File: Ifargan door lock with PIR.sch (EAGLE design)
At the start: 41 parts, among them K1 Relay, K2 Relay, Q1 2N2905, Q2 2N2219, T1 PAD_TERMINAL-4.1MMROUND, T10 PAD_TERMINAL-4.1MMROUND, T11 PAD_TERMINAL-4.1MMROUND, T12 PAD_TERMINAL-4.1MMROUND, T13 PAD_TERMINAL-4.1MMROUND, T14 PAD_TERMINAL-4.1MMROUND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

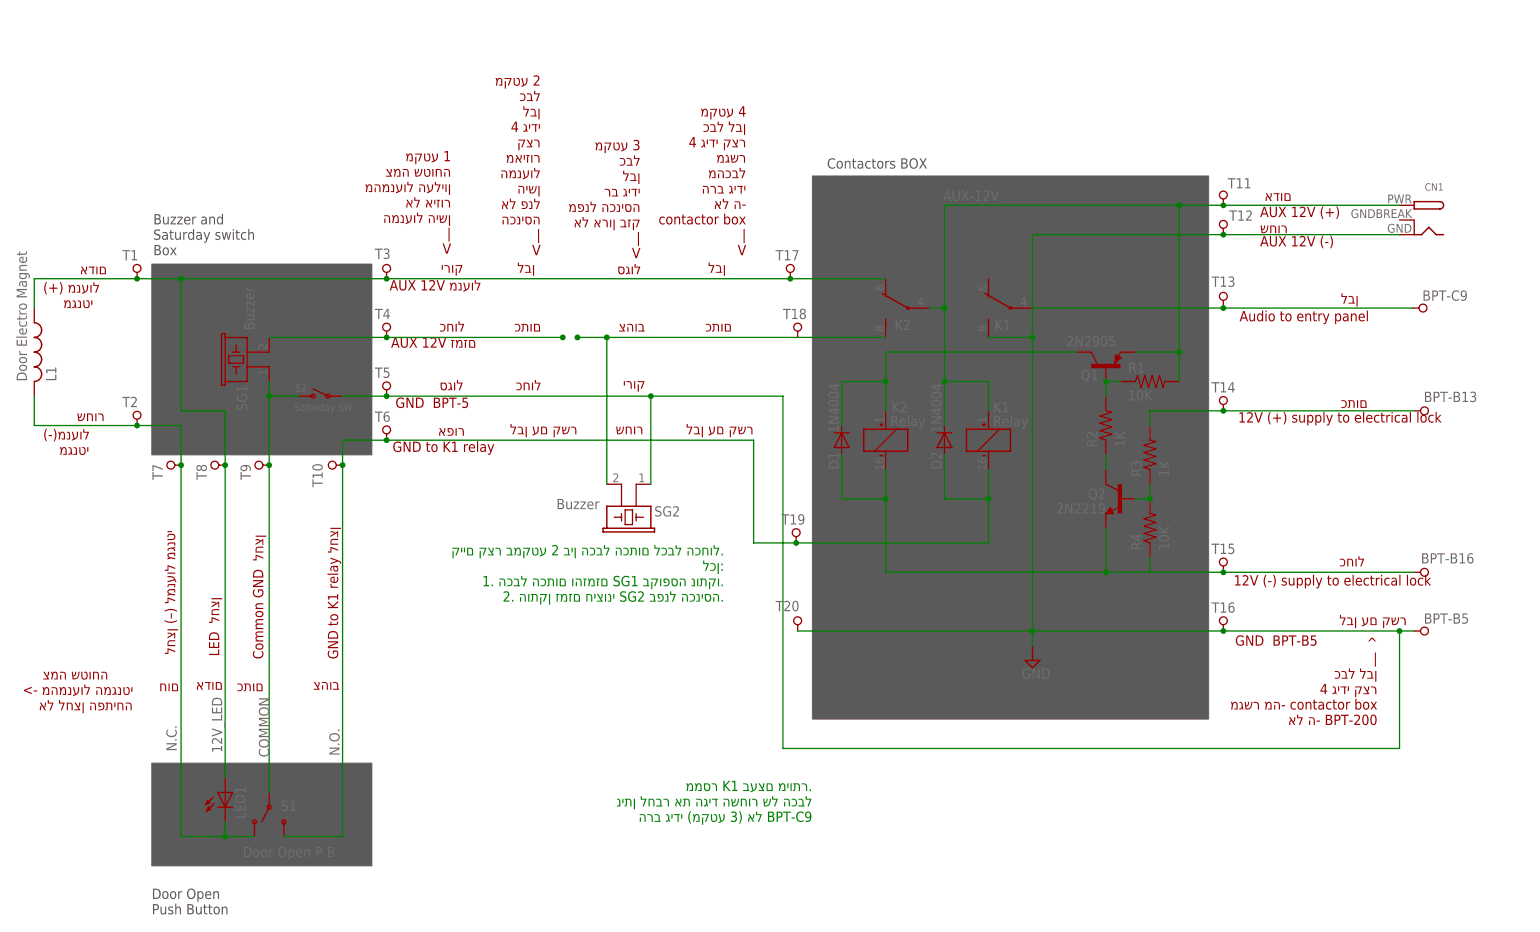
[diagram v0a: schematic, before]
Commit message: Final working design
Installed on the front door at 01-01-2015
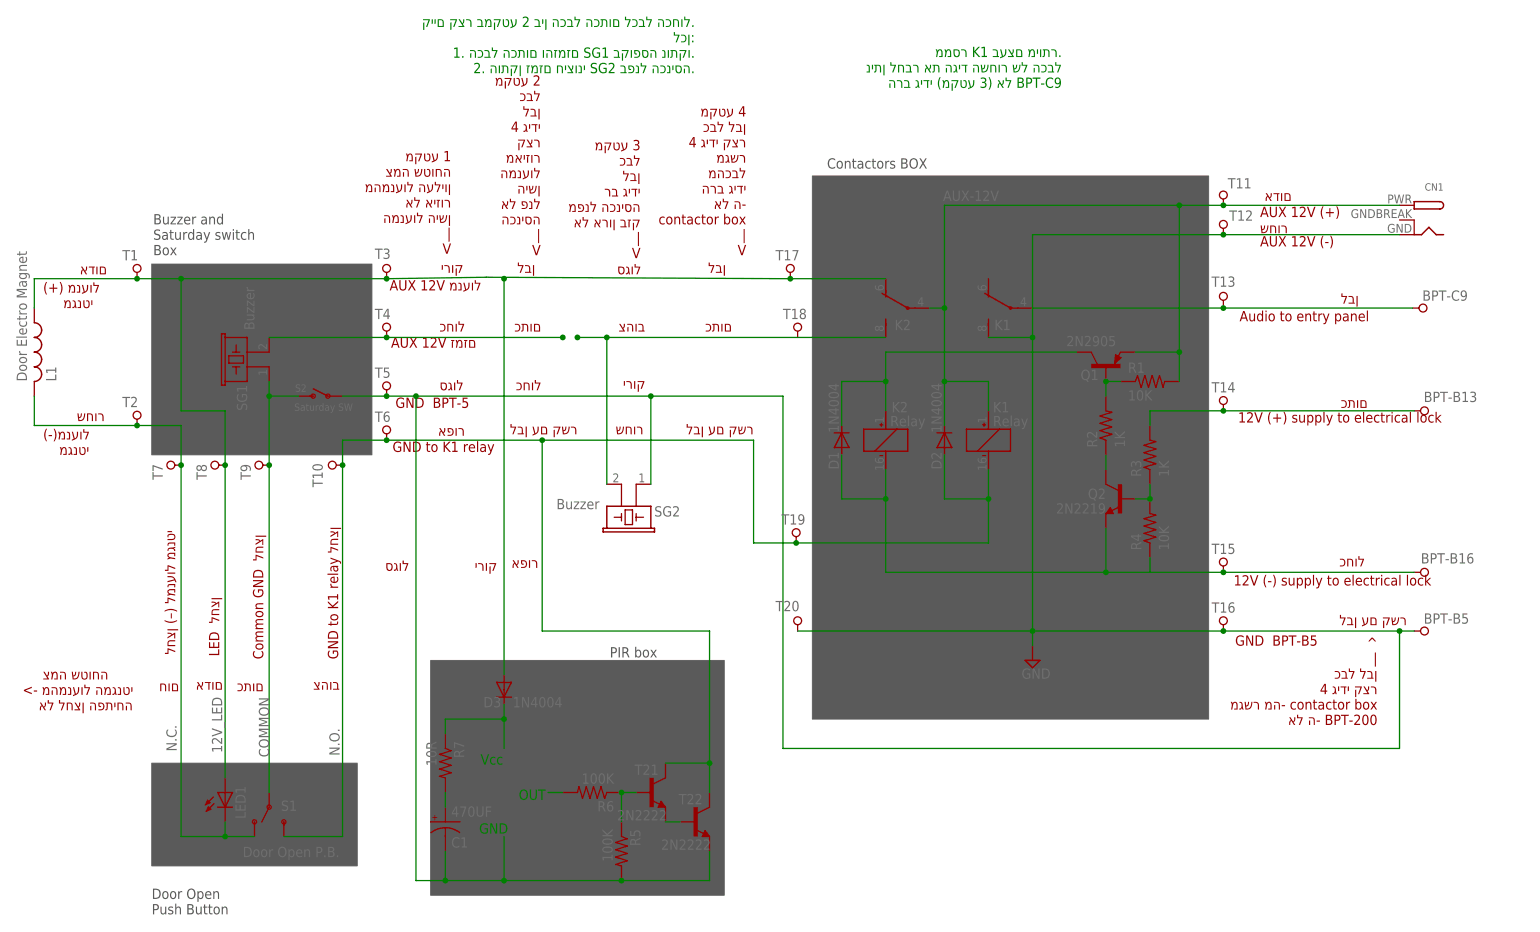
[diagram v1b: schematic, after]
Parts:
- added C1: 470UF, SparkFun-Passives:CAP_POL1206
- added D3: 1N4004, adafruit:1N4004
- added R5, R6: 100K, resistor:R-US_0207/15
- added R7: 10R, resistor:R-US_0207/15
- added T21, T22: 2N2222, adafruit:2N2222
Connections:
- new net N$10: D3.C, R7.1
- new net N$11: R6.2
- new net N$12: T21.E, T22.B
- new net N$13: D3.A
- new net N$14: R5.1, R6.1, T21.B
- new net N$15: C1.+, R7.2
- net GND: now also C1.-, R5.2, T22.E
- net N.O.: now also T21.C, T22.C
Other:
- note added: "GND"
- note added: "OUT"
- note added: "PIR Sensor"
- note added: "PIR box"
- note added: "Vcc"
